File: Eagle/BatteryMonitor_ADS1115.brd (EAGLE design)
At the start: 60.6 x 49.5 mm, 21 parts, among them IC1 MCP1703CB

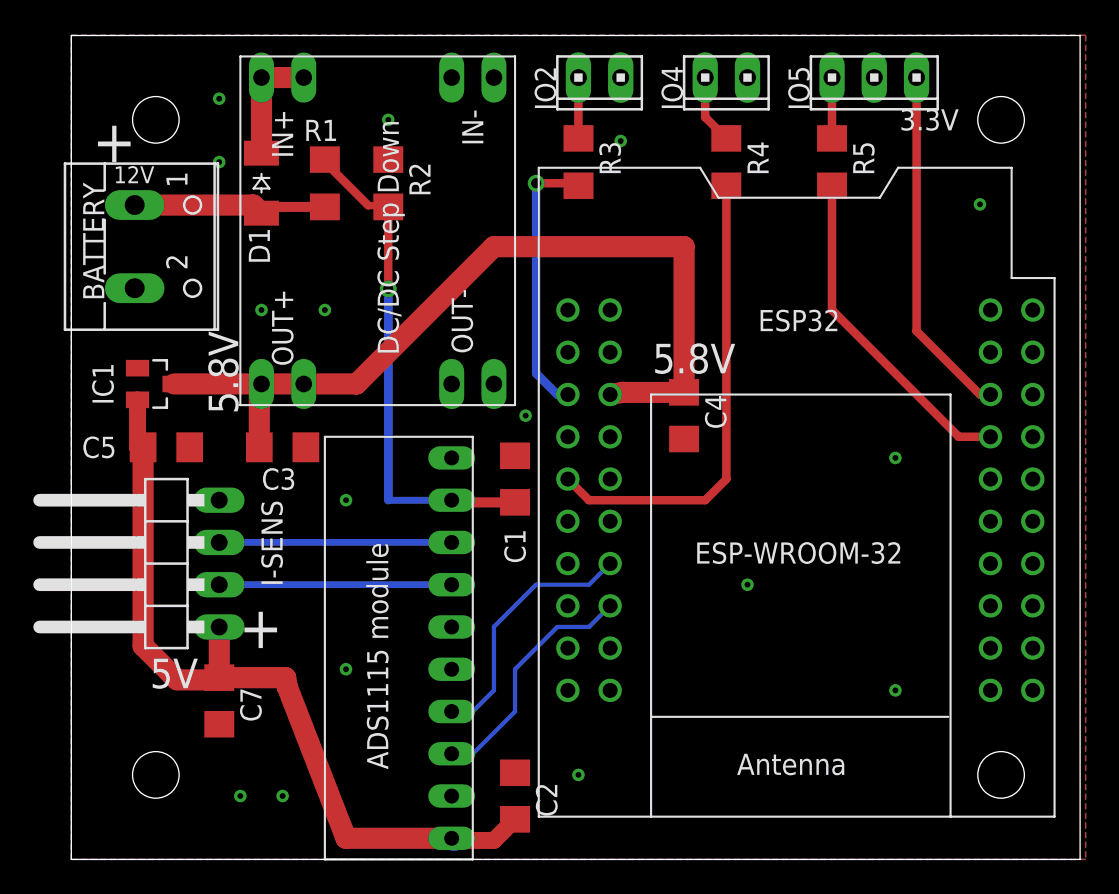
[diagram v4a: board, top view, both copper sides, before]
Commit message: Calibration done and documented
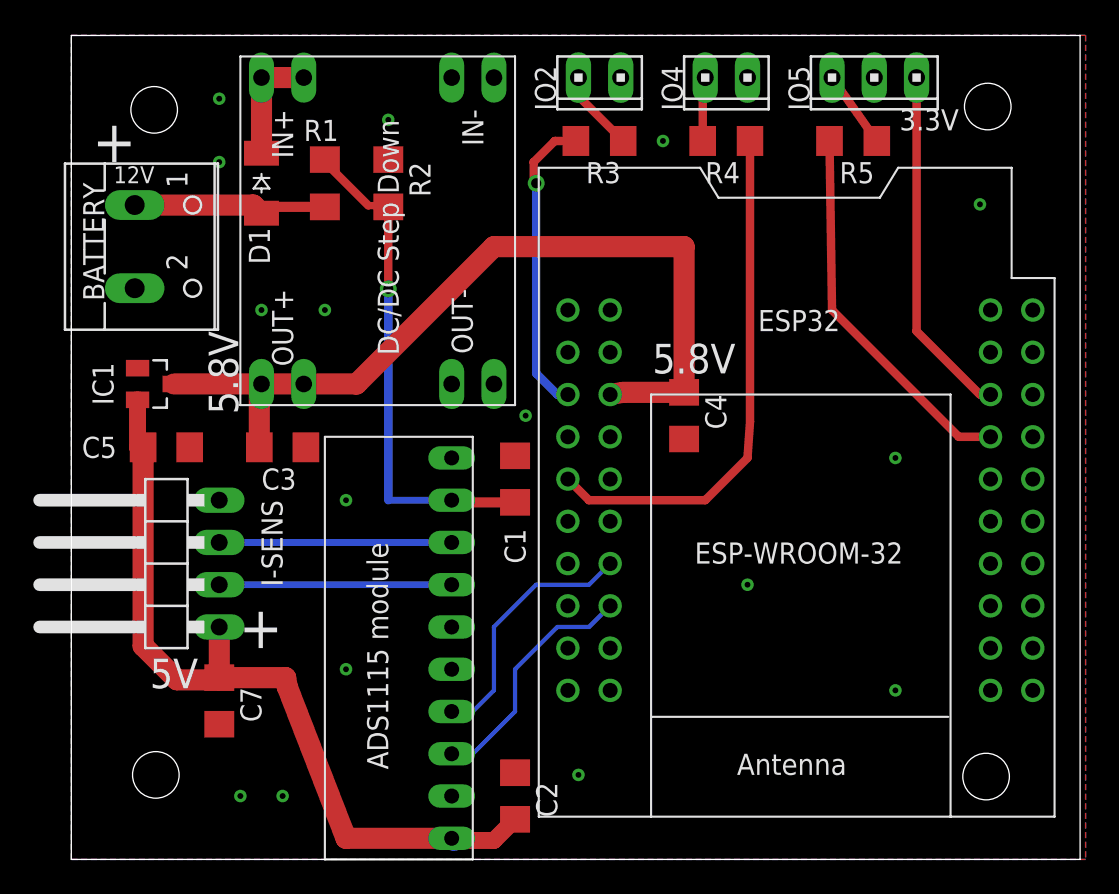
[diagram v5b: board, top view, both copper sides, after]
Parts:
- R1: value 33k -> 30k
- moved R5 1.80 mm to (47.0, 43.2), turned to 180 degrees
- moved R3 1.80 mm to (31.8, 43.2), turned to 180 degrees
- moved R4 1.27 mm to (39.4, 43.2), turned to 0 degrees
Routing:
- net N$3: track 28.2 -> 31.4 mm
- net N$5: track 20.1 -> 22.8 mm
- net N$2: track 16.5 -> 18.3 mm
- net N$11: track 3.66 -> 4.92 mm
- net N$1: track 3.66 -> 4.67 mm
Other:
- board text added: "Battery Monitor V2 CZ 2023"
- board text removed: "Battery Monitor V2 CZ 2022"
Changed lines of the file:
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@@
 <setting verticaltext="up"/>
 </settings>
-<grid distance="0.05" unitdist="inch" unit="inch" style="lines" multiple="1" display="no" altdistance="0.025" altunitdist="inch" altunit="inch"/>
+<grid distance="0.05" unitdist="inch" unit="mm" style="lines" multiple="1" display="no" altdistance="0.1" altunitdist="mm" altunit="mm"/>
 <layers>
 <layer number="1" name="Top" color="4" fill="1" visible="yes" active="yes"/>
@@
 <layer number="43" name="vRestrict" color="2" fill="10" visible="no" active="yes"/>
 <layer number="44" name="Drills" color="7" fill="1" visible="no" active="yes"/>
-<layer number="45" name="Holes" color="7" fill="1" visible="no" active="yes"/>
+<layer number="45" name="Holes" color="7" fill="1" visible="yes" active="yes"/>
 <layer number="46" name="Milling" color="3" fill="1" visible="no" active="yes"/>
 <layer number="47" name="Measures" color="7" fill="1" visible="no" active="yes"/>
@@
 <wire x1="60.63" y1="49.52" x2="0" y2="49.52" width="0" layer="20"/>
 <wire x1="0" y1="49.52" x2="0" y2="0" width="0" layer="20"/>
-<hole x="5.08" y="44.45" drill="2.8"/>
-<hole x="55.88" y="44.45" drill="2.8"/>
-<hole x="55.88" y="5.08" drill="2.8"/>
+<hole x="4.98" y="45.05" drill="2.8"/>
+<hole x="55.08" y="45.25" drill="2.8"/>
+<hole x="54.98" y="4.98" drill="2.8"/>
 <hole x="5.08" y="5.08" drill="2.8"/>
 <rectangle x1="7.62" y1="36.83" x2="10.16" y2="39.37" layer="42"/>
@@
 <text x="7.62" y="12.065" size="1.778" layer="25" rot="R180">5V</text>
 <text x="50.8" y="35.56" size="1.016" layer="26" font="vector" rot="MR0">Battery Monitor V2
-CZ 2022</text>
+CZ 2023</text>
 <text x="2.54" y="40.64" size="1.016" layer="25" font="vector">12V</text>
 <text x="34.925" y="29.21" size="1.778" layer="25">5.8V</text>
@@
 <element name="U$2" library="monitor_components" package="ADS1115" value="ADS1115MINI-MODULE" x="20.32" y="13.97" smashed="yes" rot="R270"/>
 <element name="U$3" library="monitor_components" package="DCDC-MINI" value="DCDC-MINI" x="21.59" y="38.1" smashed="yes" rot="R270"/>
-<element name="R1" library="eagle-ltspice" package="R1206" value="33k" x="15.24" y="40.64" smashed="yes" rot="R270">
+<element name="R1" library="eagle-ltspice" package="R1206" value="30k" x="15.24" y="40.64" smashed="yes" rot="R270">
 <attribute name="NAME" x="13.97" y="43.18" size="1.27" layer="25"/>
 <attribute name="SPICEMODEL" value="NONE" x="15.24" y="40.64" size="1.778" layer="27" rot="R270" display="off"/>
@@
 <attribute name="VALUE" x="50.8061" y="44.8391" size="1.27" layer="27" rot="R180"/>
 </element>
-<element name="R3" library="eagle-ltspice" package="R1206" value="1k" x="30.48" y="41.91" smashed="yes" rot="R270">
-<attribute name="NAME" x="31.75" y="43.18" size="1.27" layer="25" rot="R270"/>
-<attribute name="SPICEMODEL" value="NONE" x="30.48" y="41.91" size="1.778" layer="27" rot="R270" display="off"/>
-<attribute name="SPICEPREFIX" value="R" x="30.48" y="41.91" size="1.778" layer="27" rot="R270" display="off"/>
-<attribute name="VALUE" x="27.94" y="43.18" size="1.27" layer="27" rot="R270"/>
-</element>
-<element name="R4" library="eagle-ltspice" package="R1206" value="1k" x="39.37" y="41.91" smashed="yes" rot="R270">
-<attribute name="NAME" x="40.64" y="43.18" size="1.27" layer="25" rot="R270"/>
-<attribute name="SPICEMODEL" value="NONE" x="39.37" y="41.91" size="1.778" layer="27" rot="R270" display="off"/>
-<attribute name="SPICEPREFIX" value="R" x="39.37" y="41.91" size="1.778" layer="27" rot="R270" display="off"/>
-<attribute name="VALUE" x="36.83" y="43.18" size="1.27" layer="27" rot="R270"/>
-</element>
-<element name="R5" library="eagle-ltspice" package="R1206" value="1k" x="45.72" y="41.91" smashed="yes" rot="R270">
-<attribute name="NAME" x="46.99" y="43.18" size="1.27" layer="25" rot="R270"/>
-<attribute name="SPICEMODEL" value="NONE" x="45.72" y="41.91" size="1.778" layer="27" rot="R270" display="off"/>
-<attribute name="SPICEPREFIX" value="R" x="45.72" y="41.91" size="1.778" layer="27" rot="R270" display="off"/>
-<attribute name="VALUE" x="43.18" y="43.18" size="1.27" layer="27" rot="R270"/>
+<element name="R3" library="eagle-ltspice" package="R1206" value="1k" x="31.75" y="43.18" smashed="yes" rot="R180">
+<attribute name="NAME" x="33.02" y="41.91" size="1.27" layer="25" rot="R180"/>
+<attribute name="SPICEMODEL" value="NONE" x="31.75" y="43.18" size="1.778" layer="27" rot="R180" display="off"/>
+<attribute name="SPICEPREFIX" value="R" x="31.75" y="43.18" size="1.778" layer="27" rot="R180" display="off"/>
+<attribute name="VALUE" x="33.02" y="45.72" size="1.27" layer="27" rot="R180"/>
+</element>
+<element name="R4" library="eagle-ltspice" package="R1206" value="1k" x="39.37" y="43.18" smashed="yes">
+<attribute name="NAME" x="38.1" y="40.64" size="1.27" layer="25"/>
+<attribute name="SPICEMODEL" value="NONE" x="39.37" y="43.18" size="1.778" layer="27" display="off"/>
+<attribute name="SPICEPREFIX" value="R" x="39.37" y="43.18" size="1.778" layer="27" display="off"/>
+<attribute name="VALUE" x="38.1" y="40.64" size="1.27" layer="27"/>
+</element>
+<element name="R5" library="eagle-ltspice" package="R1206" value="1k" x="46.99" y="43.18" smashed="yes" rot="R180">
+<attribute name="NAME" x="48.26" y="41.91" size="1.27" layer="25" rot="R180"/>
+<attribute name="SPICEMODEL" value="NONE" x="46.99" y="43.18" size="1.778" layer="27" rot="R180" display="off"/>
+<attribute name="SPICEPREFIX" value="R" x="46.99" y="43.18" size="1.778" layer="27" rot="R180" display="off"/>
+<attribute name="VALUE" x="48.26" y="45.72" size="1.27" layer="27" rot="R180"/>
 </element>
 </elements>
@@
 <via x="49.53" y="24.13" extent="1-16" drill="0.35"/>
 <via x="54.61" y="39.37" extent="1-16" drill="0.35"/>
-<via x="33.02" y="43.18" extent="1-16" drill="0.35"/>
+<via x="35.56" y="43.18" extent="1-16" drill="0.35"/>
 <via x="11.43" y="33.02" extent="1-16" drill="0.35"/>
 <via x="15.24" y="33.02" extent="1-16" drill="0.35"/>
@@
 <wire x1="40.64" y1="46.99" x2="48.26" y2="46.99" width="0" layer="19" extent="1-1"/>
 <wire x1="33.02" y1="46.99" x2="40.64" y2="46.99" width="0" layer="19" extent="1-1"/>
-<wire x1="33.02" y1="43.18" x2="33.02" y2="46.99" width="0" layer="19" extent="1-1"/>
+<wire x1="35.56" y1="43.18" x2="33.02" y2="46.99" width="0" layer="19" extent="1-1"/>
 <wire x1="25.4" y1="46.99" x2="33.02" y2="46.99" width="0" layer="19" extent="1-1"/>
 <wire x1="22.86" y1="46.99" x2="25.4" y2="46.99" width="0" layer="19" extent="1-1"/>
@@
 <contactref element="ESP32" pad="IO2"/>
 <contactref element="R3" pad="2"/>
-<wire x1="30.48" y1="40.488" x2="30.328" y2="40.64" width="0.508" layer="1"/>
-<wire x1="30.328" y1="40.64" x2="27.94" y2="40.64" width="0.508" layer="1"/>
+<wire x1="30.328" y1="43.18" x2="29.058" y2="43.18" width="0.508" layer="1"/>
+<wire x1="29.058" y1="43.18" x2="27.788" y2="41.91" width="0.508" layer="1"/>
+<wire x1="27.788" y1="41.91" x2="27.788" y2="40.792" width="0.508" layer="1"/>
+<wire x1="27.788" y1="40.792" x2="27.94" y2="40.64" width="0.508" layer="1"/>
 <via x="27.94" y="40.64" extent="1-16" drill="0.6096"/>
 <wire x1="27.94" y1="40.64" x2="27.94" y2="29.21" width="0.508" layer="16"/>
@@
 <contactref element="ESP32" pad="IO4"/>
 <contactref element="R4" pad="2"/>
-<wire x1="39.37" y1="22.86" x2="38.1" y2="21.59" width="0.508" layer="1"/>
+<wire x1="40.64" y1="24.13" x2="38.1" y2="21.59" width="0.508" layer="1"/>
 <wire x1="31.115" y1="21.59" x2="29.845" y2="22.86" width="0.508" layer="1"/>
-<wire x1="39.37" y1="40.488" x2="39.37" y2="22.86" width="0.508" layer="1"/>
+<wire x1="40.792" y1="43.18" x2="40.792" y2="26.302040625" width="0.508" layer="1"/>
+<wire x1="40.792" y1="26.302040625" x2="40.64" y2="24.13" width="0.508" layer="1"/>
 <wire x1="38.1" y1="21.59" x2="31.115" y2="21.59" width="0.508" layer="1"/>
 </signal>
@@
 <contactref element="ESP32" pad="IO5"/>
 <contactref element="R5" pad="2"/>
-<wire x1="45.72" y1="40.488" x2="45.72" y2="33.02" width="0.508" layer="1"/>
+<wire x1="45.568" y1="43.18" x2="45.72" y2="33.02" width="0.508" layer="1"/>
 <wire x1="45.72" y1="33.02" x2="53.34" y2="25.4" width="0.508" layer="1"/>
 <wire x1="53.34" y1="25.4" x2="55.245" y2="25.4" width="0.508" layer="1"/>
@@
 <contactref element="IO4" pad="1"/>
 <contactref element="R4" pad="1"/>
-<wire x1="38.1" y1="46.99" x2="38.1" y2="44.602" width="0.508" layer="1"/>
-<wire x1="39.37" y1="43.332" x2="38.1" y2="44.602" width="0.508" layer="1"/>
+<wire x1="38.1" y1="46.99" x2="37.948" y2="46.838" width="0.508" layer="1"/>
+<wire x1="37.948" y1="43.18" x2="37.948" y2="46.838" width="0.508" layer="1"/>
 </signal>
 <signal name="N$11">
 <contactref element="IO2" pad="1"/>
 <contactref element="R3" pad="1"/>
-<wire x1="30.48" y1="43.332" x2="30.48" y2="46.99" width="0.508" layer="1"/>
+<wire x1="33.172" y1="43.18" x2="30.6056125" y2="45.7463875" width="0.508" layer="1"/>
+<wire x1="30.6056125" y1="45.7463875" x2="30.58554375" y2="46.24945625" width="0.508" layer="1"/>
+<wire x1="30.58554375" y1="46.24945625" x2="30.48" y2="46.355" width="0.508" layer="1"/>
+<wire x1="30.48" y1="46.355" x2="30.48" y2="46.99" width="0.508" layer="1"/>
 </signal>
 <signal name="N$1">
 <contactref element="R5" pad="1"/>
 <contactref element="IO5" pad="1"/>
-<wire x1="45.72" y1="46.99" x2="45.72" y2="43.332" width="0.508" layer="1"/>
+<wire x1="45.72" y1="46.99" x2="48.412" y2="43.18" width="0.508" layer="1"/>
 </signal>
 <signal name="N$12">
